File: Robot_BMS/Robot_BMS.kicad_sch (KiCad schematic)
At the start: 0 parts

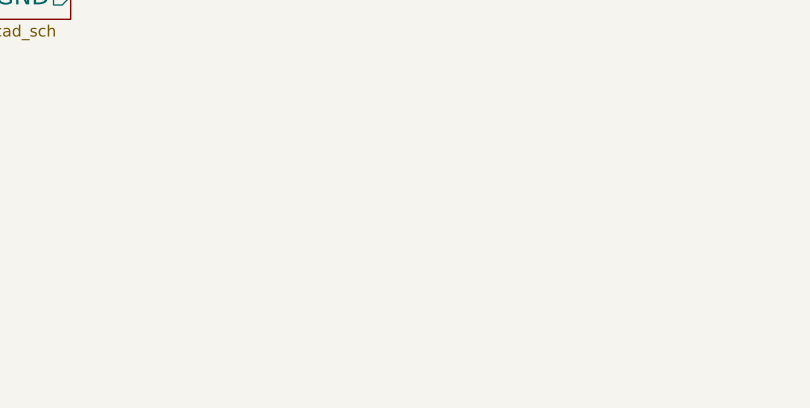
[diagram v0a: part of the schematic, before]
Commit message: switching usb c pd chip to ap33772 due to better support online
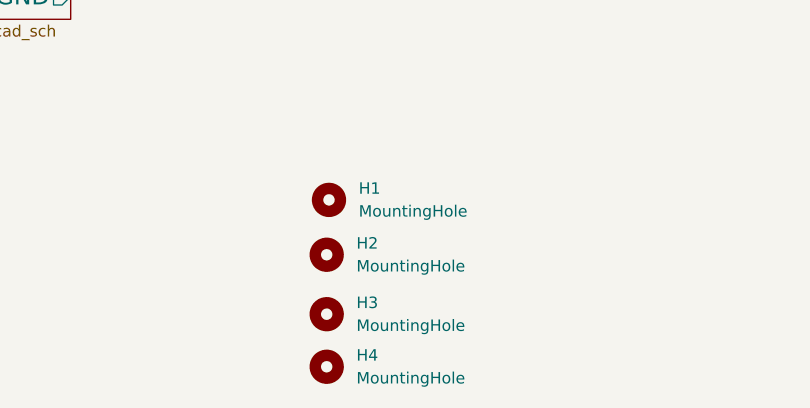
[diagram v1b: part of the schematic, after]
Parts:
- added H1, H2, H3, H4: MountingHole, MountingHole:MountingHole_3.2mm_M3, symbol Mechanical:MountingHole

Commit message: mid way implementing new usb-pd chip
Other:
- sheet Charging Circuit ports: added USB_C; removed VBUS
- sheet USB-C ports: added USB_C; removed VBUS
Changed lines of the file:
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@@
 			)
 		)
-		(pin "VBUS" output
+		(pin "USB_C" output
 			(at 230.124 134.112 180)
 			(effects
@@
 			)
 		)
-		(pin "VBUS" output
+		(pin "USB_C" output
 			(at 230.378 65.024 180)
 			(effects
 				(font
 					(size 1.905 1.905)
-					(color 255 255 255 1)
 				)
 				(justify left)

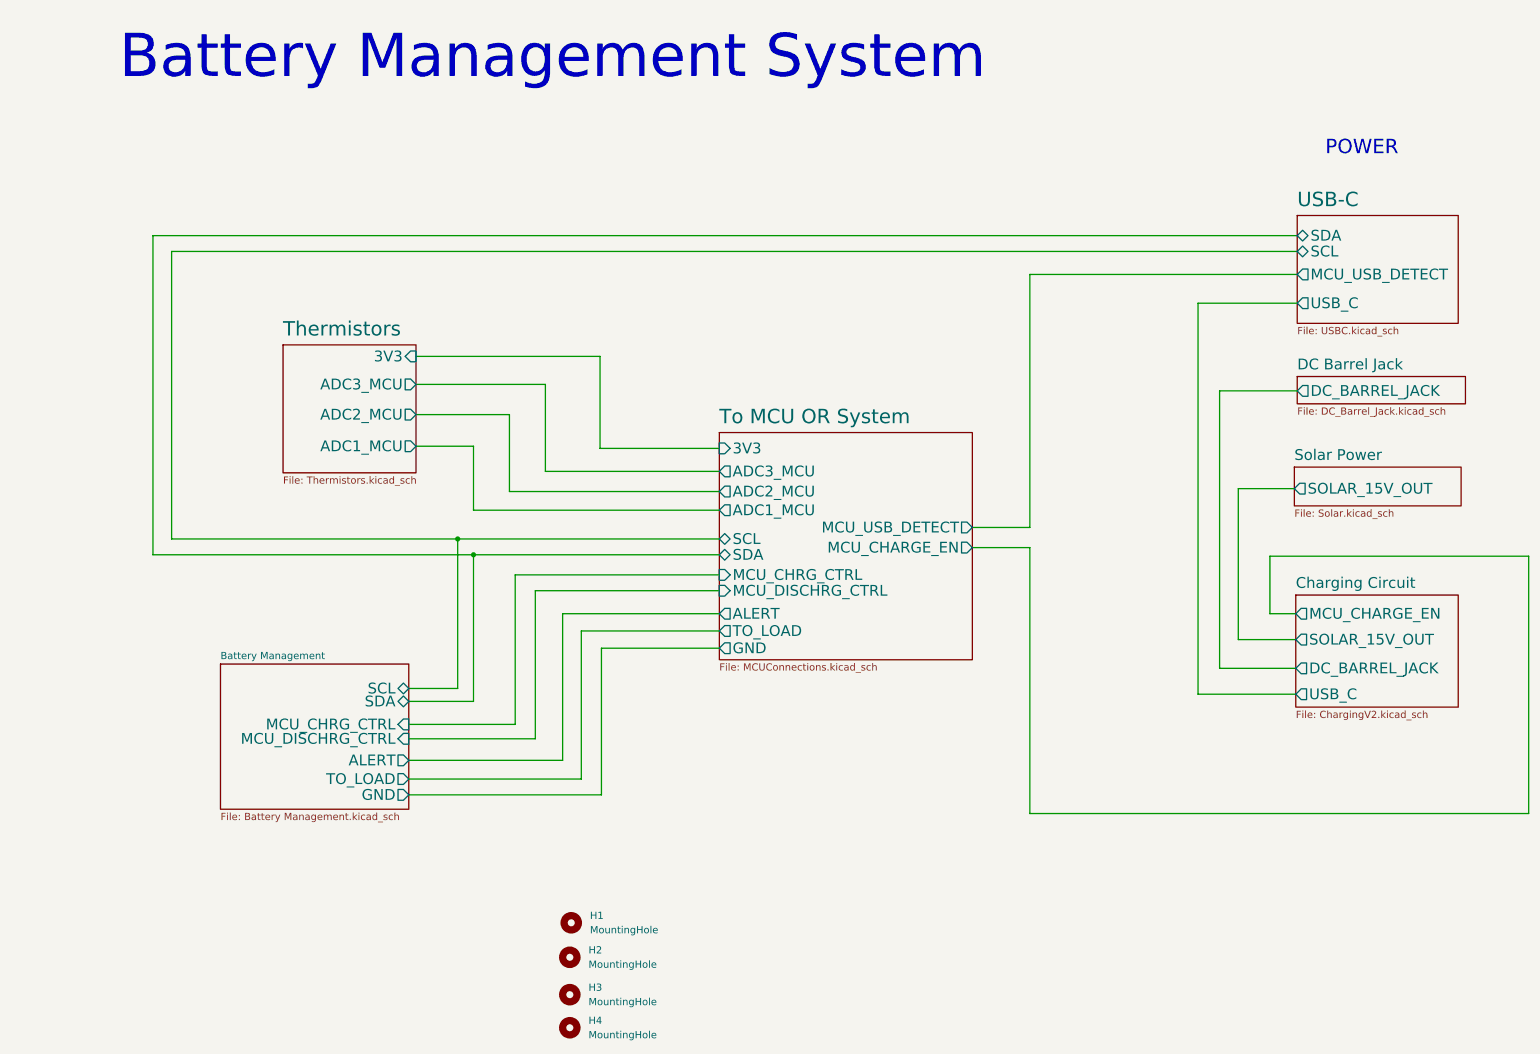
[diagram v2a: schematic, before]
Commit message: placed connectors for BMS PCB
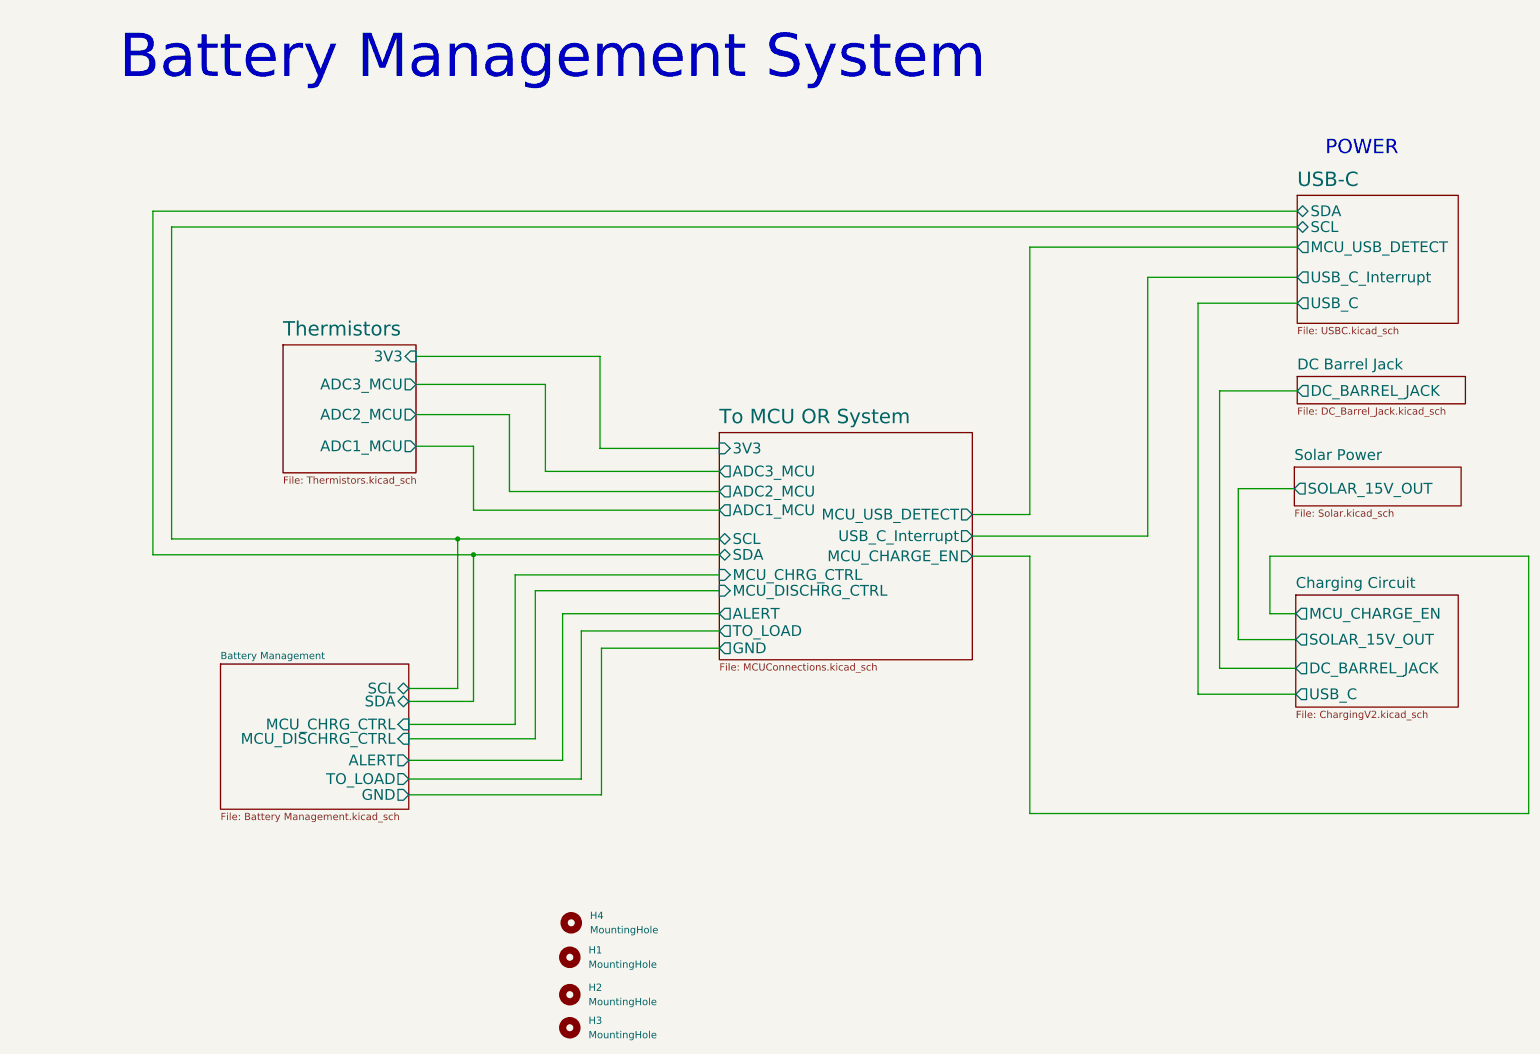
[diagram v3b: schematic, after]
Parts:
- renumbered H2 to H1, H3 to H2, H4 to H3, H1 to H4
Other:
- sheet To MCU OR System ports: added USB_C_Interrupt; removed none
- sheet USB-C ports: added USB_C_Interrupt; removed none
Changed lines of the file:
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@@
+	(wire
+		(pts
+			(xy 203.962 60.452) (xy 230.378 60.452)
+		)
+		(stroke
+			(width 0)
+			(type default)
+		)
+	)
 	(wire
 		(pts
@@
 	(wire
 		(pts
-			(xy 172.974 108.204) (xy 183.134 108.204)
+			(xy 172.974 109.728) (xy 183.134 109.728)
 		)
 		(stroke
@@
 	(wire
 		(pts
-			(xy 31.496 55.88) (xy 31.496 106.68)
+			(xy 31.496 51.562) (xy 31.496 106.68)
 		)
 		(stroke
@@
 	(wire
 		(pts
+			(xy 172.974 106.172) (xy 203.962 106.172)
+		)
+		(stroke
+			(width 0)
+			(type default)
+		)
+	)
+	(wire
+		(pts
 			(xy 97.536 79.375) (xy 74.676 79.375)
 		)
@@
 	(wire
 		(pts
-			(xy 183.134 108.204) (xy 183.134 155.194)
+			(xy 183.134 109.728) (xy 183.134 155.194)
 		)
 		(stroke
@@
 	(wire
 		(pts
-			(xy 230.378 53.086) (xy 28.194 53.086)
-		)
-		(stroke
-			(width 0)
-			(type default)
-		)
-	)
-	(wire
-		(pts
-			(xy 183.134 104.648) (xy 172.974 104.648)
+			(xy 230.378 48.768) (xy 28.194 48.768)
+		)
+		(stroke
+			(width 0)
+			(type default)
+		)
+	)
+	(wire
+		(pts
+			(xy 183.134 102.362) (xy 172.974 102.362)
 		)
 		(stroke
@@
 	(wire
 		(pts
-			(xy 230.378 59.944) (xy 183.134 59.944)
+			(xy 230.378 55.118) (xy 183.134 55.118)
 		)
 		(stroke
@@
 	(wire
 		(pts
+			(xy 203.962 106.172) (xy 203.962 60.452)
+		)
+		(stroke
+			(width 0)
+			(type default)
+		)
+	)
+	(wire
+		(pts
 			(xy 212.852 134.112) (xy 230.124 134.112)
 		)
@@
 	(wire
 		(pts
-			(xy 230.378 55.88) (xy 31.496 55.88)
+			(xy 230.378 51.562) (xy 31.496 51.562)
 		)
 		(stroke
@@
 	(wire
 		(pts
-			(xy 28.194 53.086) (xy 28.194 109.474)
-		)
-		(stroke
-			(width 0)
-			(type default)
-		)
-	)
-	(wire
-		(pts
-			(xy 183.134 59.944) (xy 183.134 104.648)
+			(xy 28.194 48.768) (xy 28.194 109.474)
+		)
+		(stroke
+			(width 0)
+			(type default)
+		)
+	)
+	(wire
+		(pts
+			(xy 183.134 55.118) (xy 183.134 102.362)
 		)
 		(stroke
@@
 		(dnp no)
 		(fields_autoplaced yes)
-		(property "Reference" "H3"
+		(property "Reference" "H2"
 			(at 105.156 185.9279 0)
 			(effects
@@
 			(project "Robot_BMS"
 				(path "/72551b1c-3d40-4199-8911-e5b015f4abec"
-					(reference "H3")
+					(reference "H2")
 					(unit 1)
 				)
@@
 		(dnp no)
 		(fields_autoplaced yes)
-		(property "Reference" "H2"
+		(property "Reference" "H1"
 			(at 105.156 179.3239 0)
 			(effects
@@
 			(project "Robot_BMS"
 				(path "/72551b1c-3d40-4199-8911-e5b015f4abec"
-					(reference "H2")
+					(reference "H1")
 					(unit 1)
 				)
@@
 		(dnp no)
 		(fields_autoplaced yes)
-		(property "Reference" "H1"
+		(property "Reference" "H4"
 			(at 105.41 173.2279 0)
 			(effects
@@
 			(project ""
 				(path "/72551b1c-3d40-4199-8911-e5b015f4abec"
-					(reference "H1")
+					(reference "H4")
 					(unit 1)
 				)
@@
 		(dnp no)
 		(fields_autoplaced yes)
-		(property "Reference" "H4"
+		(property "Reference" "H3"
 			(at 105.156 191.7699 0)
 			(effects
@@
 			(project "Robot_BMS"
 				(path "/72551b1c-3d40-4199-8911-e5b015f4abec"
-					(reference "H4")
+					(reference "H3")
 					(unit 1)
 				)
@@
 	)
 	(sheet
-		(at 230.378 49.53)
-		(size 28.448 19.05)
+		(at 230.378 45.974)
+		(size 28.448 22.606)
 		(fields_autoplaced yes)
 		(stroke
@@
 		)
 		(property "Sheetname" "USB-C"
-			(at 230.378 48.1834 0)
+			(at 230.378 44.6274 0)
 			(effects
 				(font
@@
 		)
 		(pin "MCU_USB_DETECT" output
-			(at 230.378 59.944 180)
+			(at 230.378 55.118 180)
 			(effects
 				(font
@@
 		)
 		(pin "SDA" bidirectional
-			(at 230.378 53.086 180)
+			(at 230.378 48.768 180)
 			(effects
 				(font
@@
 		)
 		(pin "SCL" bidirectional
-			(at 230.378 55.88 180)
+			(at 230.378 51.562 180)
 			(effects
 				(font
@@
 		(pin "USB_C" output
 			(at 230.378 65.024 180)
+			(effects
+				(font
+					(size 1.905 1.905)
+				)
+				(justify left)
+			)
+		)
+		(pin "USB_C_Interrupt" output
+			(at 230.378 60.452 180)
 			(effects
 				(font
@@
 		)
 		(pin "MCU_CHARGE_EN" output
-			(at 172.974 108.204 0)
+			(at 172.974 109.728 0)
 			(effects
 				(font
@@
 		)
 		(pin "MCU_USB_DETECT" output
-			(at 172.974 104.648 0)
+			(at 172.974 102.362 0)
 			(effects
 				(font
@@
 			)
 		)
+		(pin "USB_C_Interrupt" output
+			(at 172.974 106.172 0)
+			(effects
+				(font
+					(size 1.905 1.905)
+				)
+				(justify right)
+			)
+		)

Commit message: halfway throgh battery management pcb layout
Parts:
- H1, H2, H3, H4: now left out of the parts list
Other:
- sheet Battery Management ports: added TO_LOAD_GND; removed GND
- sheet To MCU OR System ports: added TO_LOAD_GND; removed GND
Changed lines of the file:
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@@
 		(unit 1)
 		(exclude_from_sim yes)
-		(in_bom yes)
+		(in_bom no)
 		(on_board yes)
 		(dnp no)
@@
 		)
 		(property "Description" "Mounting Hole without connection"
+			(at 101.854 187.198 0)
+			(effects
+				(font
+					(size 1.27 1.27)
+				)
+				(hide yes)
+			)
+		)
+		(property "Chip1Stop Part Number" ""
+			(at 101.854 187.198 0)
+			(effects
+				(font
+					(size 1.27 1.27)
+				)
+				(hide yes)
+			)
+		)
+		(property "Chip1Stop Price/Stock" ""
 			(at 101.854 187.198 0)
 			(effects
@@
 		(unit 1)
 		(exclude_from_sim yes)
-		(in_bom yes)
+		(in_bom no)
 		(on_board yes)
 		(dnp no)
@@
 		)
 		(property "Description" "Mounting Hole without connection"
+			(at 101.854 180.594 0)
+			(effects
+				(font
+					(size 1.27 1.27)
+				)
+				(hide yes)
+			)
+		)
+		(property "Chip1Stop Part Number" ""
+			(at 101.854 180.594 0)
+			(effects
+				(font
+					(size 1.27 1.27)
+				)
+				(hide yes)
+			)
+		)
+		(property "Chip1Stop Price/Stock" ""
 			(at 101.854 180.594 0)
 			(effects
@@
 		(unit 1)
 		(exclude_from_sim yes)
-		(in_bom yes)
+		(in_bom no)
 		(on_board yes)
 		(dnp no)
@@
 		)
 		(property "Description" "Mounting Hole without connection"
+			(at 102.108 174.498 0)
+			(effects
+				(font
+					(size 1.27 1.27)
+				)
+				(hide yes)
+			)
+		)
+		(property "Chip1Stop Part Number" ""
+			(at 102.108 174.498 0)
+			(effects
+				(font
+					(size 1.27 1.27)
+				)
+				(hide yes)
+			)
+		)
+		(property "Chip1Stop Price/Stock" ""
 			(at 102.108 174.498 0)
 			(effects
@@
 		(unit 1)
 		(exclude_from_sim yes)
-		(in_bom yes)
+		(in_bom no)
 		(on_board yes)
 		(dnp no)
@@
 		)
 		(property "Description" "Mounting Hole without connection"
+			(at 101.854 193.04 0)
+			(effects
+				(font
+					(size 1.27 1.27)
+				)
+				(hide yes)
+			)
+		)
+		(property "Chip1Stop Part Number" ""
+			(at 101.854 193.04 0)
+			(effects
+				(font
+					(size 1.27 1.27)
+				)
+				(hide yes)
+			)
+		)
+		(property "Chip1Stop Price/Stock" ""
 			(at 101.854 193.04 0)
 			(effects
@@
 			)
 		)
-		(pin "GND" output
+		(pin "TO_LOAD_GND" output
 			(at 73.406 151.892 0)
 			(effects
@@
 			)
 		)
-		(pin "GND" output
-			(at 128.27 125.984 180)
-			(effects
-				(font
-					(size 1.905 1.905)
-				)
-				(justify left)
-			)
-		)
 		(pin "ALERT" output
 			(at 128.27 119.888 180)
@@
 			)
 		)
+		(pin "TO_LOAD_GND" output
+			(at 128.27 125.984 180)
+			(effects
+				(font
+					(size 1.905 1.905)
+				)
+				(justify left)
+			)
+		)
